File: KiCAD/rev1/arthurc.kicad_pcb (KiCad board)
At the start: 2 copper layers, 63.5 x 30.5 mm, 54 parts, among them IC1 ATMEGA328, P1 I/O, P10 CD2, P11 CD2, P12 CD1, P13 CD1, P14 I/O, P15 I/O, P16 I/O, P2 BAT, P4 CONN_6, P5 CONN_6, P6 LiPo, P7 GPS, P8 FTDI, P9 ISP, SW1 SW_PUSH, U1 3V3, U4 DS3231N, X1 8MHz

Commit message: ArthurC rev1 (FTDI ver) complete.
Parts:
- added G***: LOGO, ArthurC Lib:OSHW_6mm, B.Cu at (29.5, 49.6)
- added G1: Logo-WL3, ArthurC Lib:Logo-WL3, F.Cu at (29.7, 28.6)
- X1: footprint ArthurC Lib:Xtal_SMD3 -> ArthurC Lib:Xtal_SMD4
- moved C11 6.28 mm to (55.9, 27.9), turned to 0 degrees
- moved X1 1.29 mm to (58.2, 31.9)
- moved C10 0.76 mm to (60.1, 27.9), turned to 0 degrees
- moved P2 0.57 mm to (82.1, 31.8)
- moved P6 0.25 mm to (79.1, 31.8)
- moved P9 0.25 mm to (47.2, 30.0)
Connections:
- net /PC1 renamed /A1
- net /PC2 renamed /A2
- net Net-(B1-Pad1) renamed /AREF
- net Net-(B8-Pad1) renamed /A7
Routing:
- net /PB7: track 7.22 -> 11.6 mm
- net /PB6: track 13.5 -> 17.1 mm
- net /RESET: track 99.1 -> 98.4 mm
- net +3.3V: track 292.1 -> 291.6 mm
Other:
- board text added: "A1"
- board text added: "A2"
- board text added: "A7"
- board text added: "AREF"
- board text added: "BAT 9V max"
- board text added: "LiPo 3V7 max"
- board text removed: "ADC 7"
- board text removed: "PC1"
- board text removed: "PC2"

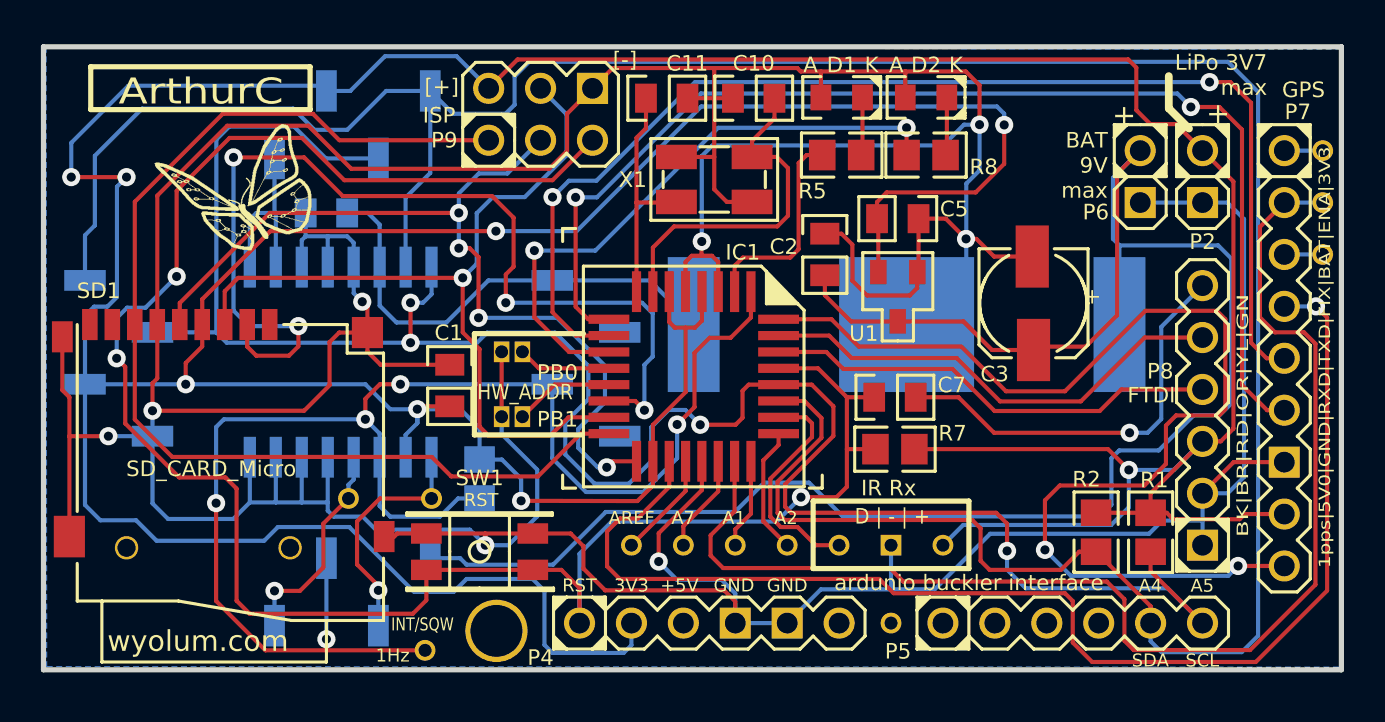
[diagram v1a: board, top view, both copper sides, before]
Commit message: ArthurC rev1 ready. Added LED breakout pads
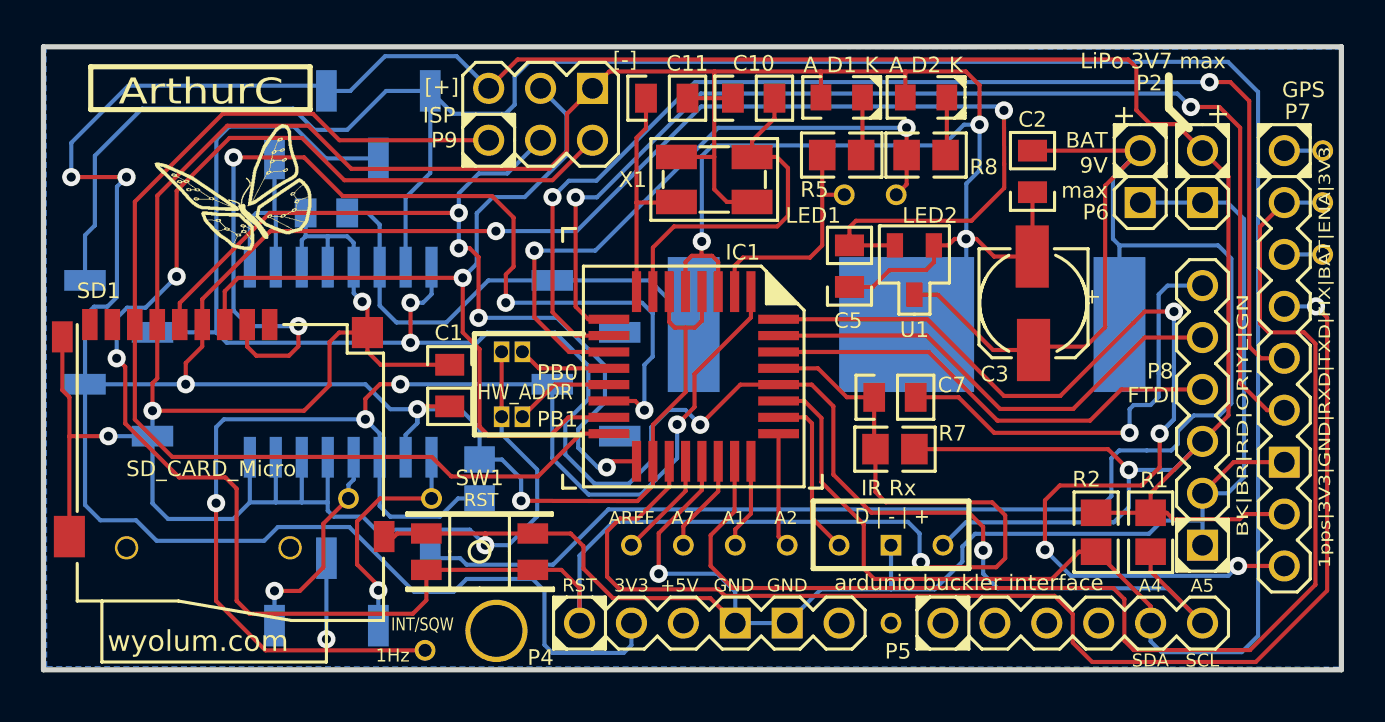
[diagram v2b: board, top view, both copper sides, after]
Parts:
- added LED1: I/O, ArthurC Lib:I%2fO, F.Cu at (64.6, 32.6)
- added LED2: I/O, ArthurC Lib:I%2fO, F.Cu at (67.1, 32.6)
- moved C2 10.9 mm to (73.8, 31.5), turned to 90 degrees
- moved C5 3.31 mm to (64.8, 36.1), turned to 90 degrees
- moved U1 1.54 mm to (68.0, 36.3)
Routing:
- net /RESET: track 98.4 -> 115.1 mm
- net /arthurc_rtc/SCL: track 103.0 -> 98.0 mm
- net /1pps: track 56.2 -> 52.6 mm, vias 2 -> 4
- net GND: track 311.6 -> 308.1 mm
- net /arthurc_rtc/SDA: track 141.4 -> 138.1 mm
- net /Ir_Dat: track 11.1 -> 8.27 mm
- net /LED2: track 29.6 -> 31.8 mm
- net +3.3V: track 291.6 -> 293.5 mm
- net /arthurc_rtc/BAT: track 116.4 -> 115.1 mm
- net /LED1: track 10.3 -> 11.5 mm
- net Net-(C7-Pad1): track 20.4 -> 21.4 mm
- net /A2: track 6.25 -> 5.63 mm
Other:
- board text added: "1pps|3V3|GND|RXD|TXD|FIX|BAT|ENA|3V3"
- board text added: "3Vgps|ENA|BAT|FIX|TXD|RXD|GND|3V3|1pps"
- board text added: "rev1"
- board text removed: "1pps|5V0|GND|RXD|TXD|FIX|BAT|ENA|3V3"
- board text removed: "3V3|ENA|BAT|FIX|TXD|RXD|GND|5V0|1pps"

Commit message: breakout pads made bigger in ArthurC_rev1
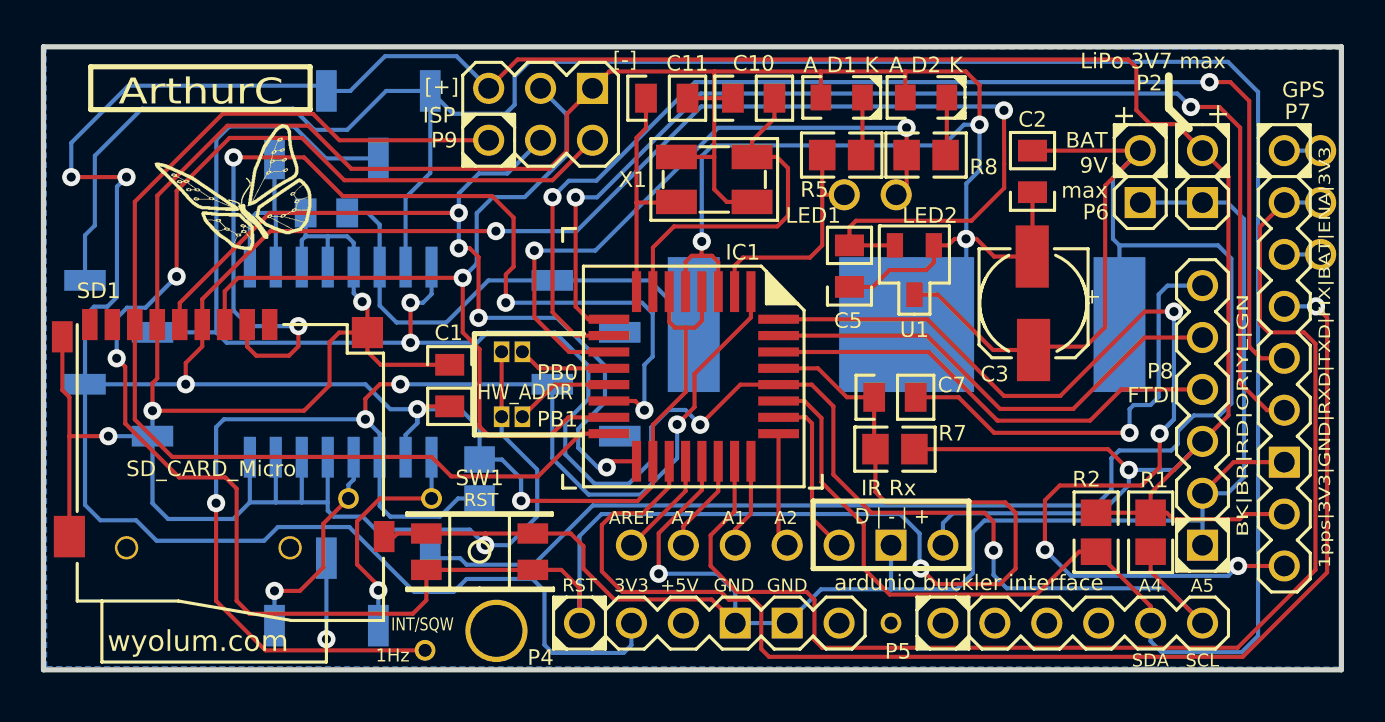
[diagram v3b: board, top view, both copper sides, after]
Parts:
- moved P14 0.10 mm to (87.9, 30.5)
- moved P15 0.10 mm to (87.9, 33.0)
- moved P16 0.10 mm to (87.9, 35.6)
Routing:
- net /RESET: track 115.1 -> 118.2 mm
- net GND: track 308.1 -> 308.9 mm
- net /EN: track 62.6 -> 62.0 mm
- net /arthurc_rtc/SDA: track 138.1 -> 138.8 mm

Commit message: final ArthurC rev1
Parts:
- moved LED1 18.3 mm to (82.1, 27.4)
- moved LED2 13.0 mm to (79.1, 27.4)
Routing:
- net /LED1: track 11.5 -> 34.3 mm
- net /arthurc_rtc/32k: track 11.7 -> 29.8 mm, vias 1 -> 2
- net /arthurc_rtc/RST: track 10.6 -> 27.0 mm, vias 1 -> 2
- net /LED2: track 31.8 -> 46.9 mm
- net /arthurc_rtc/BAT: track 114.9 -> 128.3 mm
- net /GPS_Tx: track 59.6 -> 65.8 mm
- net GND: track 308.9 -> 302.9 mm
- net /arthurc_rtc/SDA: track 138.8 -> 143.8 mm
- net /GPS_Rx: track 57.8 -> 62.7 mm
- net /SCK: track 43.5 -> 47.2 mm
- net /arthurc_rtc/SCL: track 98.2 -> 101.9 mm
- net /arthurc_rtc/SQW: track 73.1 -> 76.8 mm
- net +3.3V: track 293.5 -> 295.9 mm
- net /RESET: track 118.2 -> 116.3 mm
- net /MISO: track 55.5 -> 54.5 mm
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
